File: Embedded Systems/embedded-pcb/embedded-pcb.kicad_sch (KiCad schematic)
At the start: 11 parts, among them M1 Motor_Servo

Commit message: feat: updated schematic
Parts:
- removed A2: Arduino_Nano_v2.x, Module:Arduino_Nano, symbol MCU_Module:Arduino_Nano_v2.x
- removed M1: Motor_Servo, symbol Motor:Motor_Servo
- removed RV1, RV2, RV3: R_Potentiometer_Trim, Potentiometer_THT:Potentiometer_ACP_CA9-H2,5_Horizontal, symbol Device:R_Potentiometer_Trim
- removed Servos1: Conn_01x06, Connector_PinSocket_2.54mm:PinSocket_1x06_P2.54mm_Vertical, symbol Connector_Generic:Conn_01x06
- added J1: Servos, Connector_PinSocket_2.54mm:PinSocket_1x06_P2.54mm_Vertical, symbol Connector_Generic:Conn_01x06
- added R4, R4*1, R5, R5*1, R7, R7*1, R8, R8*1, Rsen1, Rsen2: R, Resistor_THT:R_Axial_DIN0207_L6.3mm_D2.5mm_P10.16mm_Horizontal, symbol Device:R
- added RV1, RV2: 10k, Potentiometer_THT:Potentiometer_Alps_RK163_Single_Horizontal, symbol Device:R_Potentiometer
- added U1, U2: LM324, Package_DIP:DIP-14_W7.62mm, symbol Amplifier_Operational:LM324
- D1: value Fault LED -> LED; footprint LED_THT:LED_D5.0mm_Horizontal_O1.27mm_Z9.0mm -> LED_THT:LED_D5.0mm
- D2: value Indicator LED -> LED; footprint LED_THT:LED_D5.0mm_Horizontal_O1.27mm_Z9.0mm -> LED_THT:LED_D5.0mm
- R2: value 160 -> 200
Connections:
- net GND: now also R1.2, R2.2, J1.1 (Pin_1), J1.4 (Pin_4), R5.2, R8.2, RV1.3, RV2.3; no longer D1.1 (K), D2.1 (K)
- net PWM: now also J1.3 (Pin_3), J1.6 (Pin_6)
- net Vcc: now also J1.2 (Pin_2), J1.5 (Pin_5), R4*1.1, R7*1.1, Rsen1.2, Rsen2.2; no longer A1.27 (+5V)
- net at A1.19 (A0): now also RV2.2
- net at R2.1: now also D2.1 (K); no longer D2.2 (A)
- net at A1.12 (D9): now also D1.2 (A); no longer R2.2
- net at A1.13 (D10): now also D2.2 (A); no longer R1.2
- net at A1.17 (3V3): now also RV1.1, RV2.1
- net at A1.20 (A1): now also RV1.2
- net at A1.21 (A2): now also R8*1.2, U2.1
- net at A1.22 (A3): now also R5*1.2, U1.1
- net at R1.1: now also D1.1 (K); no longer D1.2 (A)
- new net: R4*1.2, R5*1.1, U1.2 (-)
- new net: A1.27 (+5V), R4.1, R7.1, Rsen1.1, Rsen2.1
- new net: R7.2, R8.1, U2.3 (+)
- new net: R7*1.2, R8*1.1, U2.2 (-)
- new net: R4.2, R5.1, U1.3 (+)
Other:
- note added: "R4=R4*, R5=R5* R7=R7*, R8=R8* Rsen1 < R4, R5 Rsen2 < R7, R8"

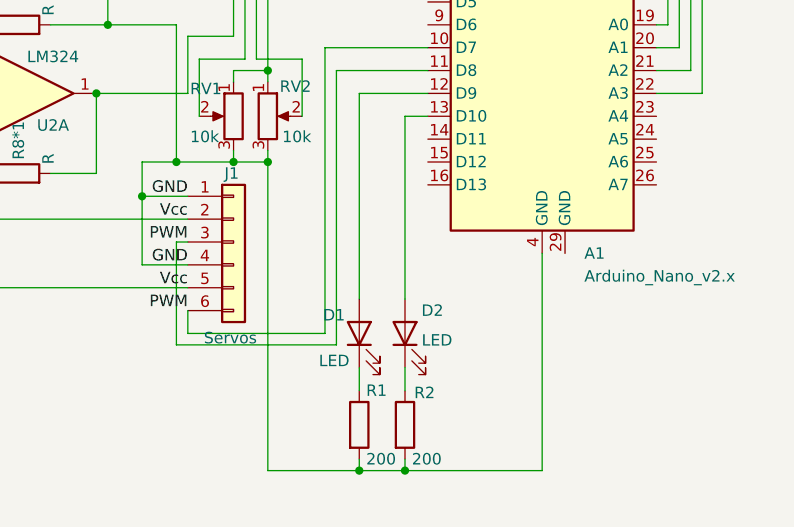
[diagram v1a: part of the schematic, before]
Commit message: feat: updated schematic for 3.3v
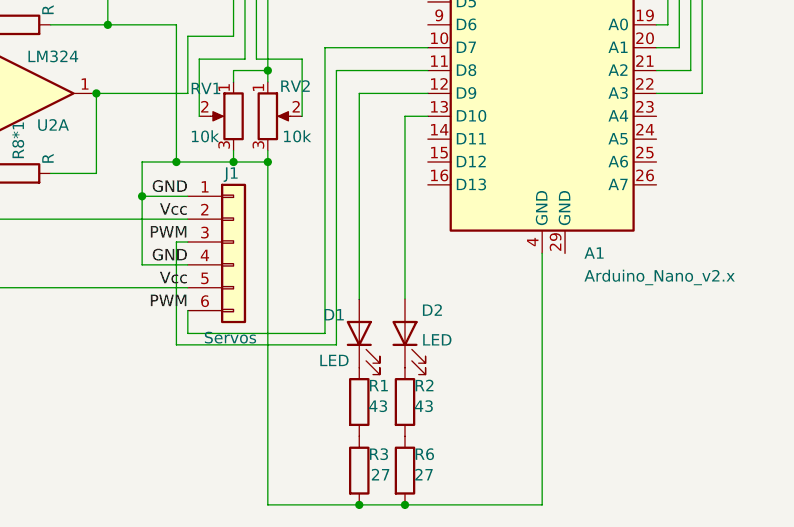
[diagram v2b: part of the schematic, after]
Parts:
- added R3, R6: 27, Resistor_THT:R_Axial_DIN0207_L6.3mm_D2.5mm_P10.16mm_Horizontal, symbol Device:R
- R1, R2: value 200 -> 43
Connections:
- net GND: now also R3.2, R6.2; no longer R1.2, R2.2
- new net: R1.2, R3.1
- new net: R2.2, R6.1
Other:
- moved on the sheet: R1, R2
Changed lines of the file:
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@@
+	)
+	(junction
+		(at 177.8 153.67)
+		(diameter 0)
+		(color 0 0 0 0)
 	)
 	(junction
@@
 	)
 	(junction
-		(at 177.8 149.86)
-		(diameter 0)
-		(color 0 0 0 0)
-	)
-	(junction
 		(at 116.84 111.76)
 		(diameter 0)
@@
 	)
 	(junction
-		(at 182.88 149.86)
+		(at 182.88 153.67)
 		(diameter 0)
 		(color 0 0 0 0)
@@
 	(wire
 		(pts
-			(xy 177.8 149.86) (xy 182.88 149.86)
-		)
-		(stroke
-			(width 0)
-			(type default)
-		)
-	)
-	(wire
-		(pts
 			(xy 167.64 73.66) (xy 200.66 73.66)
 		)
@@
 	(wire
 		(pts
-			(xy 182.88 149.86) (xy 198.12 149.86)
-		)
-		(stroke
-			(width 0)
-			(type default)
-		)
-	)
-	(wire
-		(pts
 			(xy 160.02 104.14) (xy 165.1 104.14)
 		)
@@
 	(wire
 		(pts
-			(xy 177.8 138.43) (xy 177.8 140.97)
-		)
-		(stroke
-			(width 0)
-			(type default)
-		)
-	)
-	(wire
-		(pts
 			(xy 157.48 100.33) (xy 157.48 115.57)
 		)
@@
 	(wire
 		(pts
-			(xy 182.88 138.43) (xy 182.88 140.97)
-		)
-		(stroke
-			(width 0)
-			(type default)
-		)
-	)
-	(wire
-		(pts
 			(xy 130.81 85.09) (xy 133.35 85.09)
 		)
@@
 	(wire
 		(pts
-			(xy 167.64 115.57) (xy 167.64 149.86)
+			(xy 167.64 115.57) (xy 167.64 153.67)
 		)
 		(stroke
@@
 	(wire
 		(pts
-			(xy 182.88 149.86) (xy 182.88 148.59)
+			(xy 167.64 153.67) (xy 177.8 153.67)
 		)
 		(stroke
@@
 	(wire
 		(pts
+			(xy 177.8 153.67) (xy 182.88 153.67)
+		)
+		(stroke
+			(width 0)
+			(type default)
+		)
+	)
+	(wire
+		(pts
 			(xy 116.84 104.14) (xy 123.19 104.14)
 		)
@@
 	(wire
 		(pts
-			(xy 167.64 149.86) (xy 177.8 149.86)
-		)
-		(stroke
-			(width 0)
-			(type default)
-		)
-	)
-	(wire
-		(pts
-			(xy 198.12 149.86) (xy 198.12 125.73)
+			(xy 198.12 125.73) (xy 198.12 153.67)
 		)
 		(stroke
@@
 	(wire
 		(pts
-			(xy 177.8 148.59) (xy 177.8 149.86)
-		)
-		(stroke
-			(width 0)
-			(type default)
-		)
-	)
-	(wire
-		(pts
 			(xy 157.48 135.89) (xy 175.26 135.89)
 		)
@@
 		(pts
 			(xy 135.89 116.84) (xy 133.35 116.84)
+		)
+		(stroke
+			(width 0)
+			(type default)
+		)
+	)
+	(wire
+		(pts
+			(xy 182.88 153.67) (xy 198.12 153.67)
 		)
 		(stroke
@@
 			)
 			(justify right bottom)
+		)
+	)
+	(symbol
+		(lib_id "Device:R")
+		(at 177.8 149.86 0)
+		(unit 1)
+		(exclude_from_sim no)
+		(in_bom yes)
+		(on_board yes)
+		(dnp no)
+		(property "Reference" "R3"
+			(at 178.816 148.082 0)
+			(effects
+				(font
+					(size 1.27 1.27)
+				)
+				(justify left)
+			)
+		)
+		(property "Value" "27"
+			(at 179.07 150.368 0)
+			(effects
+				(font
+					(size 1.27 1.27)
+				)
+				(justify left)
+			)
+		)
+		(property "Footprint" "Resistor_THT:R_Axial_DIN0207_L6.3mm_D2.5mm_P10.16mm_Horizontal"
+			(at 176.022 149.86 90)
+			(effects
+				(font
+					(size 1.27 1.27)
+				)
+				(hide yes)
+			)
+		)
+		(property "Datasheet" "~"
+			(at 177.8 149.86 0)
+			(effects
+				(font
+					(size 1.27 1.27)
+				)
+				(hide yes)
+			)
+		)
+		(property "Description" "Resistor"
+			(at 177.8 149.86 0)
+			(effects
+				(font
+					(size 1.27 1.27)
+				)
+				(hide yes)
+			)
+		)
+		(pin "2"
+		)
+		(pin "1"
+		)
+		(instances
+			(project "embedded-pcb"
+				(path "/59fd546b-6695-413e-ad86-d6d97541805c"
+					(reference "R3")
+					(unit 1)
+				)
+			)
 		)
 	)
@@
 	(symbol
 		(lib_id "Device:R")
-		(at 177.8 144.78 0)
+		(at 177.8 142.24 0)
 		(unit 1)
 		(exclude_from_sim no)
@@
 		(dnp no)
 		(property "Reference" "R1"
-			(at 178.562 140.97 0)
-			(effects
-				(font
-					(size 1.27 1.27)
-				)
-				(justify left)
-			)
-		)
-		(property "Value" "200"
-			(at 178.562 148.59 0)
+			(at 178.816 140.462 0)
+			(effects
+				(font
+					(size 1.27 1.27)
+				)
+				(justify left)
+			)
+		)
+		(property "Value" "43"
+			(at 178.816 142.748 0)
 			(effects
 				(font
@@
 		)
 		(property "Footprint" "Resistor_THT:R_Axial_DIN0207_L6.3mm_D2.5mm_P10.16mm_Horizontal"
-			(at 176.022 144.78 90)
+			(at 176.022 142.24 90)
 			(effects
 				(font
@@
 		)
 		(property "Datasheet" "~"
-			(at 177.8 144.78 0)
+			(at 177.8 142.24 0)
 			(effects
 				(font
@@
 		)
 		(property "Description" "Resistor"
-			(at 177.8 144.78 0)
+			(at 177.8 142.24 0)
 			(effects
 				(font
@@
 				(path "/59fd546b-6695-413e-ad86-d6d97541805c"
 					(reference "R1")
+					(unit 1)
+				)
+			)
+		)
+	)
+	(symbol
+		(lib_id "Device:R")
+		(at 182.88 149.86 0)
+		(unit 1)
+		(exclude_from_sim no)
+		(in_bom yes)
+		(on_board yes)
+		(dnp no)
+		(property "Reference" "R6"
+			(at 183.896 148.082 0)
+			(effects
+				(font
+					(size 1.27 1.27)
+				)
+				(justify left)
+			)
+		)
+		(property "Value" "27"
+			(at 183.896 150.368 0)
+			(effects
+				(font
+					(size 1.27 1.27)
+				)
+				(justify left)
+			)
+		)
+		(property "Footprint" "Resistor_THT:R_Axial_DIN0207_L6.3mm_D2.5mm_P10.16mm_Horizontal"
+			(at 181.102 149.86 90)
+			(effects
+				(font
+					(size 1.27 1.27)
+				)
+				(hide yes)
+			)
+		)
+		(property "Datasheet" "~"
+			(at 182.88 149.86 0)
+			(effects
+				(font
+					(size 1.27 1.27)
+				)
+				(hide yes)
+			)
+		)
+		(property "Description" "Resistor"
+			(at 182.88 149.86 0)
+			(effects
+				(font
+					(size 1.27 1.27)
+				)
+				(hide yes)
+			)
+		)
+		(pin "2"
+		)
+		(pin "1"
+		)
+		(instances
+			(project "embedded-pcb"
+				(path "/59fd546b-6695-413e-ad86-d6d97541805c"
+					(reference "R6")
 					(unit 1)
 				)
@@
 	(symbol
 		(lib_id "Device:R")
-		(at 182.88 144.78 0)
+		(at 182.88 142.24 0)
 		(unit 1)
 		(exclude_from_sim no)
@@
 		(dnp no)
 		(property "Reference" "R2"
-			(at 183.896 141.224 0)
-			(effects
-				(font
-					(size 1.27 1.27)
-				)
-				(justify left)
-			)
-		)
-		(property "Value" "200"
-			(at 183.642 148.59 0)
+			(at 183.896 140.462 0)
+			(effects
+				(font
+					(size 1.27 1.27)
+				)
+				(justify left)
+			)
+		)
+		(property "Value" "43"
+			(at 183.896 142.748 0)
 			(effects
 				(font
@@
 		)
 		(property "Footprint" "Resistor_THT:R_Axial_DIN0207_L6.3mm_D2.5mm_P10.16mm_Horizontal"
-			(at 181.102 144.78 90)
+			(at 181.102 142.24 90)
 			(effects
 				(font
@@
 		)
 		(property "Datasheet" "~"
-			(at 182.88 144.78 0)
+			(at 182.88 142.24 0)
 			(effects
 				(font
@@
 		)
 		(property "Description" "Resistor"
-			(at 182.88 144.78 0)
-			(effects
-				(font
+			(at 182.88 142.24 0)
+			(effects
+				(font

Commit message: feat: updated schematic
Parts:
- removed R3, R6: 27, Resistor_THT:R_Axial_DIN0207_L6.3mm_D2.5mm_P10.16mm_Horizontal, symbol Device:R
- added unit 5 of U1
- R1: renamed from R4; value R -> 220
- R2: renamed from R7; value R -> 220
- R3: renamed from R5; value R -> 1k
- R4: renamed from R8; value R -> 1k
- R4*1, R7*1: value R -> 220
- R5*1, R8*1: value R -> 1k
- Rsen1, Rsen2: value R -> 10k
- renumbered R1 to R5, R2 to R6, U2 to U1
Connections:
- net GND: now also R5.2, R6.2, U1.11 (V-)
- net at A1.27 (+5V), R1.1, R2.1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: now also U1.4 (V+)
- net at R2.2, R4.1: now also U1.5 (+); no longer U1.3 (+)
- net at A1.21 (A2), R8*1.2: now also U1.7; no longer U1.1
- net at R7*1.2, R8*1.1: now also U1.6 (-); no longer U1.2 (-)
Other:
- moved on the sheet: R5, R6

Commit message: feat: updated schematic
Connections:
- net at R4*1.2, R5*1.1: now also U1.6 (-); no longer U1.2 (-)
- net at A1.22 (A3), R5*1.2: now also U1.7; no longer U1.1
- net at R2.2, R4.1: now also U1.3 (+); no longer U1.5 (+)
- net at A1.21 (A2), R8*1.2: now also U1.1; no longer U1.7
- net at R7*1.2, R8*1.1: now also U1.2 (-); no longer U1.6 (-)
- net at R1.2, R3.1: now also U1.5 (+); no longer U1.3 (+)
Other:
- added sheet Power Management (untitled.kicad_sch)
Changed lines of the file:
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@@
 		(lib_id "Amplifier_Operational:LM324")
 		(at 140.97 107.95 0)
-		(unit 2)
+		(unit 1)
 		(exclude_from_sim no)
 		(in_bom yes)
@@
 				(path "/59fd546b-6695-413e-ad86-d6d97541805c"
 					(reference "U1")
-					(unit 2)
+					(unit 1)
 				)
 			)
@@
 		(lib_id "Amplifier_Operational:LM324")
 		(at 140.97 82.55 0)
-		(unit 1)
+		(unit 2)
 		(exclude_from_sim no)
 		(in_bom yes)
@@
 				(path "/59fd546b-6695-413e-ad86-d6d97541805c"
 					(reference "U1")
-					(unit 1)
+					(unit 2)
 				)
 			)
@@
 				)
 			)
+		)
+	)
+	(sheet
+		(at 73.66 109.22)
+		(size 36.83 46.99)
+		(exclude_from_sim no)
+		(in_bom yes)
+		(on_board yes)
+		(dnp no)
+		(fields_autoplaced yes)
+		(stroke
+			(width 0.1524)
+			(type solid)
+		)
+		(fill
+			(color 0 0 0 0.0000)
+		)
+		(property "Sheetname" "Power Management"
+			(at 73.66 108.5084 0)
+			(effects
+				(font
+					(size 1.27 1.27)
+				)
+				(justify left bottom)
+			)
+		)
+		(property "Sheetfile" "untitled.kicad_sch"
+			(at 73.66 156.7946 0)
+			(effects
+				(font
+					(size 1.27 1.27)
+				)
+				(justify left top)
+			)
+		)
+		(instances
+			(project "embedded-pcb"
+				(path "/59fd546b-6695-413e-ad86-d6d97541805c"
+					(page "2")
+				)
+			)

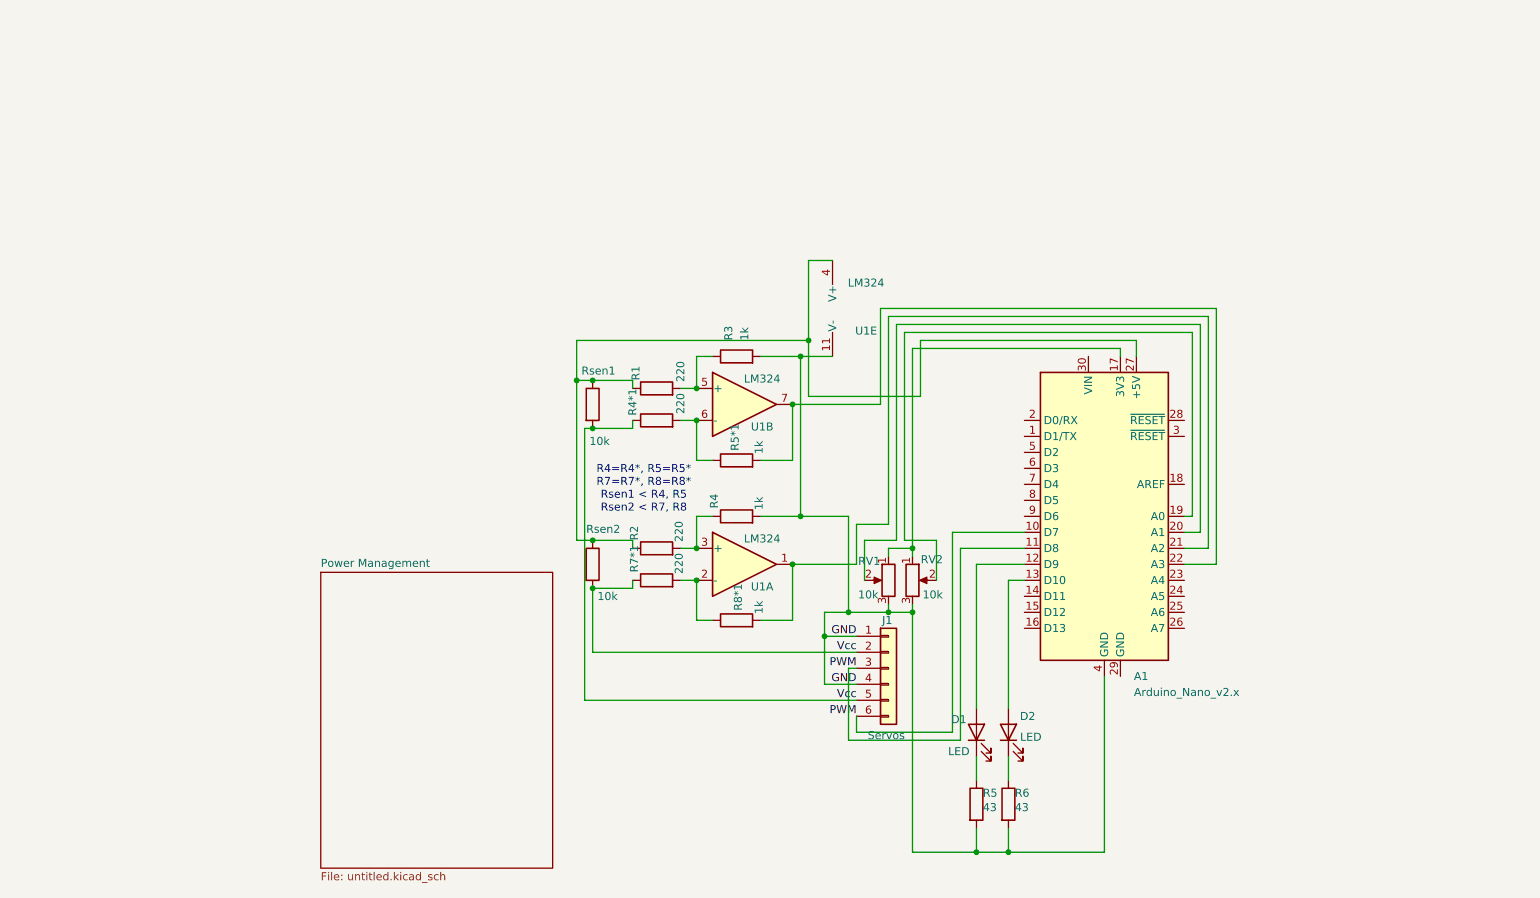
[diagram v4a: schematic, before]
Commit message: feat: v2 of PCB design
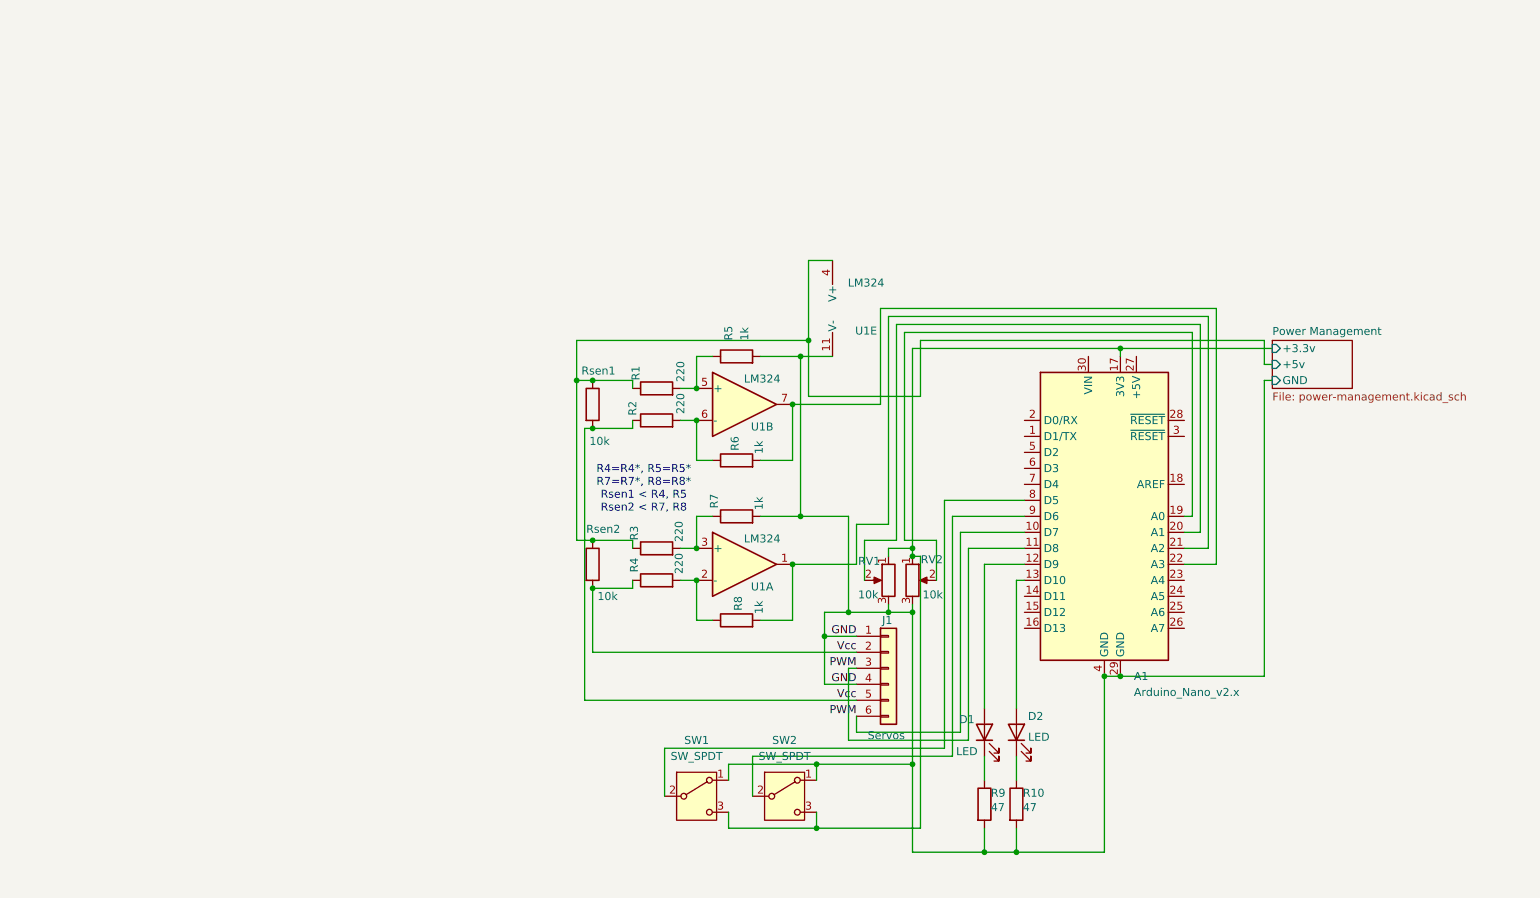
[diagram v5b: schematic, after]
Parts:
- added SW1, SW2: SW_SPDT, Connector_Wire:SolderWire-0.1sqmm_1x03_P3.6mm_D0.4mm_OD1mm, symbol Switch:SW_SPDT
- R10: renamed from R6; value 43 -> 47
- R9: renamed from R5; value 43 -> 47
- RV1, RV2: footprint Potentiometer_THT:Potentiometer_Alps_RK163_Single_Horizontal -> Connector_Wire:SolderWire-0.1sqmm_1x03_P3.6mm_D0.4mm_OD1mm
- renumbered R4*1 to R2, R2 to R3, R7*1 to R4, R3 to R5, R5*1 to R6, R4 to R7, R8*1 to R8
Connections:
- net GND: now also A1.29 (GND), SW1.1 (A), SW2.1 (A)
- net Power Management/+3.3v: now reaches A1.17 (3V3), RV1.1, RV2.1
- net Power Management/+3.3v: now also SW1.3 (C), SW2.3 (C)
- net Power Management/+5v: now reaches R1.1, R3.1, Rsen1.1, Rsen2.1, U1.4 (V+)
- net Power Management/+5v: no longer A1.27 (+5V)
- net at A1.8 (D5): now also SW1.2 (B)
- net at A1.9 (D6): now also SW2.2 (B)
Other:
- sheet Power Management: file untitled.kicad_sch -> power-management.kicad_sch
- sheet Power Management ports: added +3.3v, +5v, GND; removed none
- moved on the sheet: D1, D2, R10, R9

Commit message: feat: updated power management
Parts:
- RV1, RV2: value 10k -> 1k
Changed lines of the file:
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@@
 			)
 		)
-		(property "Value" "10k"
+		(property "Value" "1k"
 			(at 159.004 112.776 0)
 			(effects
@@
 			)
 		)
-		(property "Value" "10k"
+		(property "Value" "1k"
 			(at 172.466 112.776 0)
 			(effects
